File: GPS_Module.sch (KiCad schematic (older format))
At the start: 16 parts, among them P1 RF2-03E-T-00-50-G, Q2 BC847B, T1 FDN304P, U4 MAX-M8C

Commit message: Updated schematic
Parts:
- C34, C38: value 1uF_0603 -> 1uF/6V3
- C35, C36, C37: value 100nF_0402 -> 100nF/50V
- L5: value 39nH_0603 -> 39nH
- R18: value 100k_0402 -> 100k
- R19: value 10k_0402 -> 10k
- R20: value 47k_0402 -> 47k
- R21: value 10R_0603_1% -> 10R/1%
- R22, R23: value 2k7_0402 -> 2k7
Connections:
- net labels added: POWER_IN_1V8, POWER_IN_GND, UART_GPS_1V8_RXD
- net labels removed: NXP_UART_GPS_1V8_RXD, NXP_UART_GPS_1V8_TXD, POWER_1V8
- wire segments 47 -> 52
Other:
- note removed: "Components from this sheet are fitted in variant: full."
- note removed: "NOTE:\n-----------------\n1. Local GPS RESET is the \nsame node as Modem RESET\n(see "Modem Jumper")"
- note removed: "Note 1."
- moved on the sheet: R22, R23

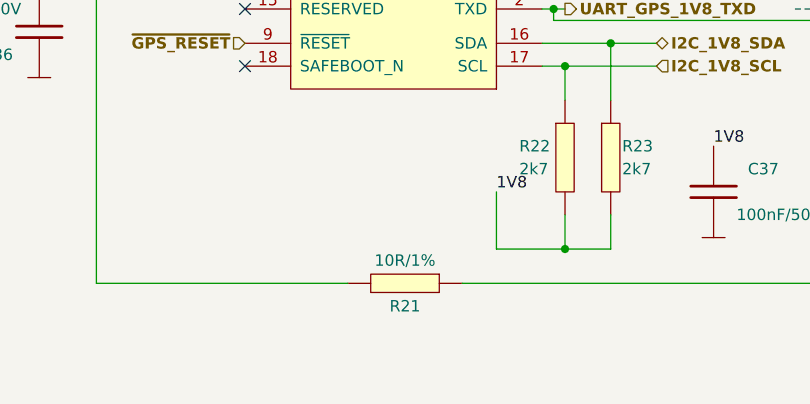
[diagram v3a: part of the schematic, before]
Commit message: Updated README.md and figurated components on pcb
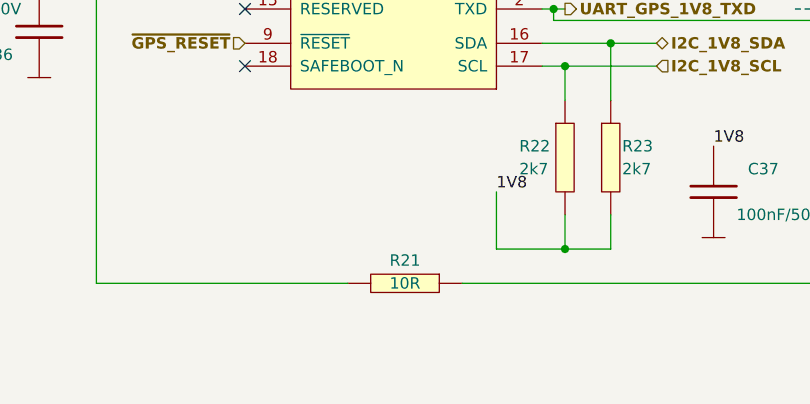
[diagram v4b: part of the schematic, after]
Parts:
- removed R21: 10R/1%, Resistor_Smd_0603:10R_0603, symbol Resistors_Smd0603:10R_0603_1%
- added R21: 10R, Resistor_Smd_0402:10R_0402, symbol Resistors_Smd0402:10R_0402
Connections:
- net at U4.14 (VCC_RF): now also R21.2
- net at C38.1, L5.2: now also R21.1
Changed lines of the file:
@@
 $Descr A3 16535 11693
 encoding utf-8
-Sheet 6 10
+Sheet 5 10
 Title "GPS UBlox Max M8C"
 Date "2020-11-21"
@@
 $EndComp
 $Comp
-L Resistors_Smd0603:10R_0603_1% R21
-U 1 1 5CD4B0B7
-P 8500 6200
-F 0 "R21" V 8600 6200 50  0000 C CNN
-F 1 "10R/1%" V 8400 6200 50  0000 C CNN
-F 2 "Resistor_Smd_0603:10R_0603" H 8750 5900 50  0001 C CNN
-F 3 "Resistors/Smd_0603/Components_Documentation/Panasonic_Precision_Resistors_SMD.pdf" H 8750 5900 50  0001 C CNN
-F 4 "ROYAL OHM" H 8500 6200 50  0001 C CNN "Manufacturer"
-F 5 "0603SAF100JT5E" H 8500 6200 50  0001 C CNN "Manufacturer Part Number"
-F 6 "TME" H 8500 6200 50  0001 C CNN "Supplier"
-F 7 "SMD0603-10R-1%" H 8500 6200 50  0001 C CNN "Supplier Part Number"
-F 8 "https://www.tme.eu/pl/details/smd0603-10r-1%2525/rezystory-smd-0603/royal-ohm/0603saf100jt5e/" H 8500 6200 50  0001 C CNN "URL"
-F 9 "0,06200" H 8500 6200 50  0001 C CNN "Price@1pc"
-F 10 "0,01694" H 8500 6200 50  0001 C CNN "Price@1000pcs"
-F 11 "-basic,+full,-minipcie" H 8500 6200 50  0001 C CNN "Variant"
-F 12 "0603" H 8500 6200 50  0001 C CNN "Package"
-	1    8500 6200
-	0    1    1    0
-$EndComp
-$Comp
 L Resistors_Smd0402:10k_0402 R19
 U 1 1 5CD565F4
@@
 Text Label 9850 5600 0    50   ~ 0
 1V8
+$Comp
+L Resistors_Smd0402:10R_0402 R21
+U 1 1 5FC68972
+P 8500 6200
+F 0 "R21" V 8400 6200 50  0000 C CNN
+F 1 "10R" V 8500 6200 50  0000 C CNN
+F 2 "Resistor_Smd_0402:10R_0402" H 9000 5750 50  0001 C CNN
+F 3 "Resistors/Smd_0402/Components_Documentation/crcw0402.pdf" H 9000 5750 50  0001 C CNN
+F 4 "ROYAL OHM" H 8500 6200 50  0001 C CNN "Manufacturer"
+F 5 "0402WGF100JTCE" H 8500 6200 50  0001 C CNN "Manufacturer Part Number"
+F 6 "TME" H 8500 6200 50  0001 C CNN "Supplier"
+F 7 "SMD0402-10R-1%" H 8500 6200 50  0001 C CNN "Supplier Part Number"
+F 8 "https://www.tme.eu/pl/details/smd0402-10r-1%2525/rezystory-smd-0402/royal-ohm/0402wgf100jtce/" H 8500 6200 50  0001 C CNN "URL"
+F 9 "0,03878" H 8500 6200 50  0001 C CNN "Price@1pc"
+F 10 "0,01044" H 8500 6200 50  0001 C CNN "Price@1000pcs"
+F 11 "0402" H 8500 6200 50  0001 C CNN "Package"
+	1    8500 6200
+	0    1    1    0
+$EndComp
 $EndSCHEMATC
